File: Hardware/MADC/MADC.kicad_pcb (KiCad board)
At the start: 2 copper layers, 20 x 20 mm, 34 parts, among them J1 Conn_02x04_Counter_Clockwise, J3 Conn_02x03_Counter_Clockwise, U1 LM311PWR, U2 OPA192IDBVT, U3 OPA140AIDBVT, U4 OPA2192IDGKT, U5 DG419LEUA, U6 DG211BDQ-T1-E3

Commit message: PCB
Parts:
- removed the C8 at (142.5, 106.9)
- added C1: 0.1u, Capacitor_SMD:C_0402_1005Metric_Pad0.74x0.62mm_HandSolder, F.Cu at (148.1, 92.2)
- added C10: 0.1u, Capacitor_SMD:C_0402_1005Metric_Pad0.74x0.62mm_HandSolder, F.Cu at (147.4, 98.6)
- added C11: 0.1u, Capacitor_SMD:C_0402_1005Metric_Pad0.74x0.62mm_HandSolder, F.Cu at (139.4, 91.6)
- added C2: 0.1u, Capacitor_SMD:C_0402_1005Metric_Pad0.74x0.62mm_HandSolder, F.Cu at (145.4, 101.7)
- added C3: 0.1u, Capacitor_SMD:C_0402_1005Metric_Pad0.74x0.62mm_HandSolder, F.Cu at (147.4, 95.5)
- added C4: 0.1u, Capacitor_SMD:C_0402_1005Metric_Pad0.74x0.62mm_HandSolder, F.Cu at (139.8, 99.9)
- added C5: 0.1u, Capacitor_SMD:C_0402_1005Metric_Pad0.74x0.62mm_HandSolder, B.Cu at (146.2, 91.9)
- C12: renamed from C2; moved to F.Cu
- C8: renamed from C7; moved to F.Cu
- D1, D2: value BAV21W-E3-08 -> 1N4448WT; footprint Diode_SMD:D_SOD-123 -> Diode_SMD:D_SOD-323
- J2: renamed from J3; footprint Connector_PinHeader_1.27mm:PinHeader_2x03_P1.27mm_Vertical_SMD -> Connector_PinHeader_1.27mm:PinHeader_2x04_P1.27mm_Vertical_SMD
- R10: renamed from R6; moved to F.Cu
- R4: renamed from R9; moved to B.Cu
- RN1: moved to B.Cu
- RN2: renamed from RN3; moved to B.Cu
- U2: renamed from U5; moved to F.Cu
- moved R1 28.9 mm to (134.9, 89.3), turned to -90 degrees
- moved R2 27.1 mm to (135.9, 93.5), turned to 180 degrees
- moved C7 25.8 mm to (138.2, 93.5), turned to 180 degrees
- moved C6 24.4 mm to (134.9, 91.6), turned to 90 degrees
- moved C9 13.4 mm to (140.1, 95.9), turned to -90 degrees
- moved C8 7.55 mm to (137.2, 88.1), turned to 180 degrees
- moved RN1 7.54 mm to (143.8, 93.3), turned to 90 degrees
- moved C12 7.11 mm to (147.3, 86.5), turned to 90 degrees
- moved R5 6.16 mm to (146.3, 86.5), turned to 90 degrees
- moved C13 6.04 mm to (140.1, 86.2)
- moved R6 5.89 mm to (141.1, 86.2), turned to 90 degrees
- moved U4 4.38 mm to (137.2, 90.9), turned to 90 degrees
- moved R11 3.96 mm to (149.2, 96.6)
- moved RN2 3.92 mm to (143.8, 99.4), turned to 180 degrees
- moved R10 3.91 mm to (151.5, 96.6), turned to -90 degrees
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- renumbered C3 to C13, C4 to C14, C1 to C15, C5 to C6, C6 to C7, R11 to R1, R5 to R11, R4 to R12, R12 to R2, R10 to R3, R7 to R5, R8 to R6, R2 to R7, R1 to R8, R3 to R9, RN2 to RN3, U6 to U1, U4 to U3, U3 to U4, U2 to U5, U1 to U6
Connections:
- J1 pad 2: /AD_IRN -> +3.3V
- J1 pad 3: /AD_ID -> /AD_CMP
- J1 pad 4: /AD_IIN -> /AD_IRN
- J1 pad 6: /AD_IRP -> /AD_IIN
- J1 pad 7: /AD_CMP -> /AD_IRP
- J1 pad 8: +3.3V -> /AD_ID
- J2 pad 2: /AD_IN -> GNDA
- J2 pad 3: GNDA -> /AD_IN
- J2 pad 4: VCC -> GNDA
- J2 pad 5: VEE -> /AD_IN
- J2 pad 6: -7V -> VCC
- U2 pad 1: unconnected-(U5-Pad1) -> Net-(U3A-+)
- U3 pad 3: unconnected-(U4A-+-Pad3) -> Net-(U3A-+)
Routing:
- net VCC: track 0.00 -> 57.4 mm, vias 0 -> 6
- net VEE: track 0.00 -> 46.3 mm, vias 0 -> 6
- net +3.3V: track 0.00 -> 40.4 mm, vias 0 -> 6
- net GNDA: track 0.00 -> 31.1 mm, vias 0 -> 20
- net Net-(C8-Pad2): track 0.00 -> 31.0 mm, vias 0 -> 2
- net Net-(U4--): track 0.00 -> 25.1 mm
- net /AD_REF+: track 0.00 -> 20.9 mm, vias 0 -> 1
- net /AD_REF-: track 0.00 -> 17.0 mm, vias 0 -> 1
- net /AD_IN: track 0.00 -> 16.2 mm
- net /AD_IRN: track 0.00 -> 16.2 mm, vias 0 -> 1
- net Net-(D1-A): track 0.00 -> 15.7 mm, vias 0 -> 1
- net Net-(D1-K): track 0.00 -> 15.1 mm, vias 0 -> 2
- net /AD_IIN: track 0.00 -> 13.8 mm, vias 0 -> 1
- net -7V: track 0.00 -> 13.8 mm, vias 0 -> 1
- net /SW_VRH: track 0.00 -> 13.5 mm, vias 0 -> 1
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- added copper zone on B.Cu, net +3.3V
- added copper zone on In2.Cu, net +3.3V
- added copper zone on B.Cu, net GNDA
- added copper zone on F.Cu, net GNDA
- added copper zone on In1.Cu, net GNDA
- added copper zone on B.Cu, net GNDD
- added copper zone on F.Cu, net GNDD
- added copper zone on In1.Cu, net GNDD
- added copper zone on In2.Cu, net VCC
- added copper zone on In2.Cu, net VEE
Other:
- copper layers 2 -> 4

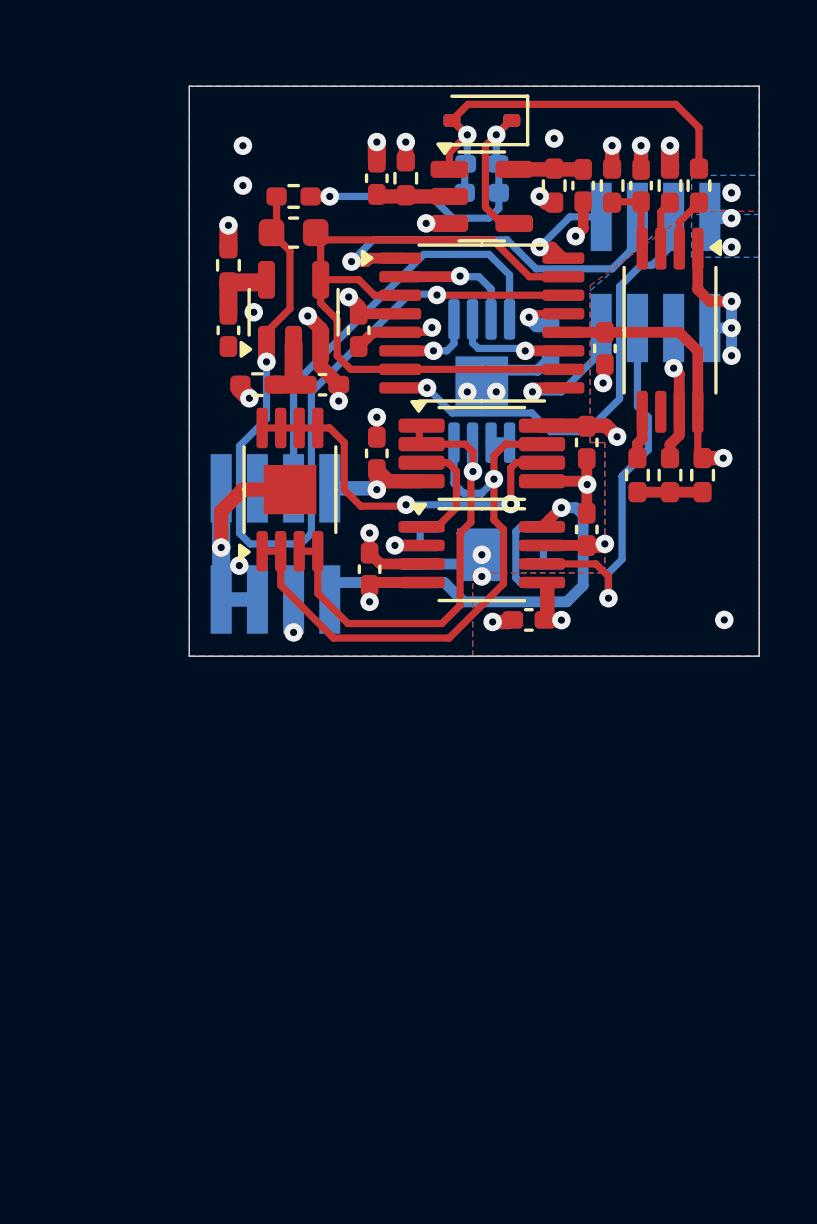
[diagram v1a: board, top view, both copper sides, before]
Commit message: MADC module send to production
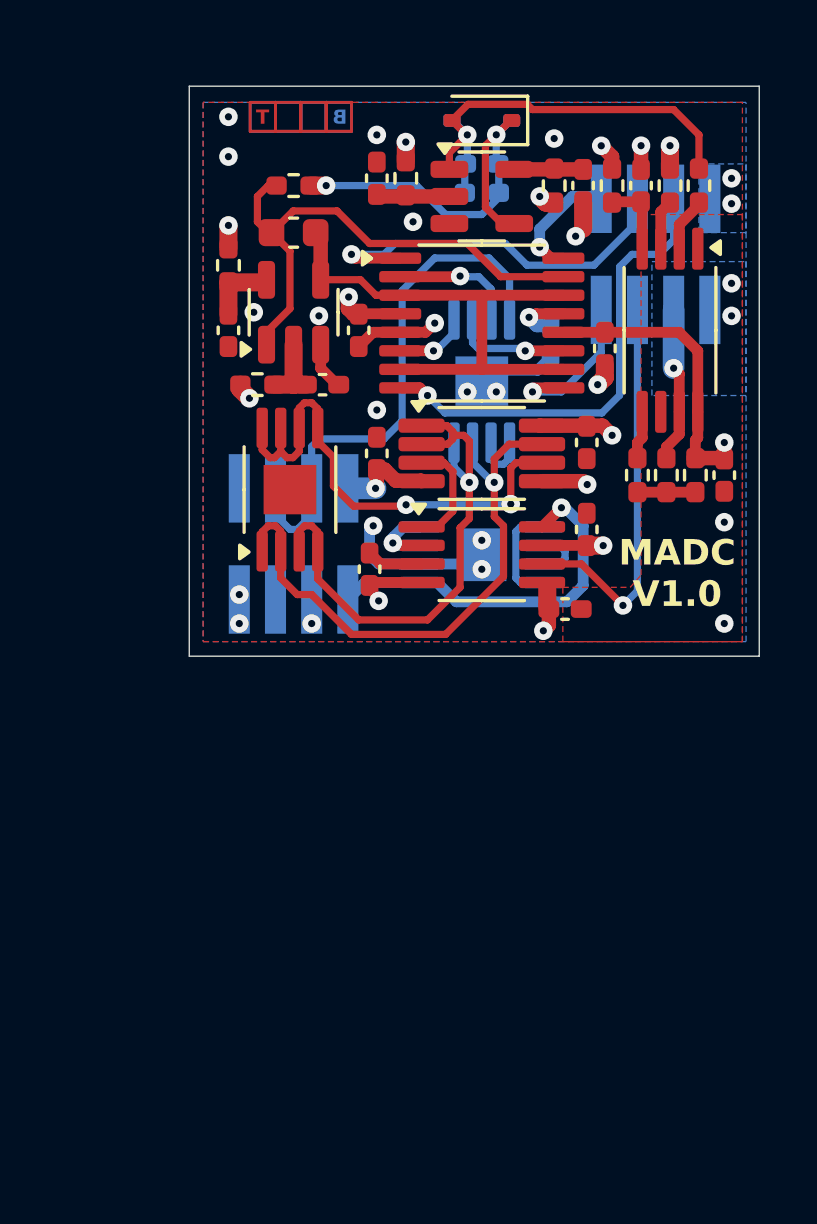
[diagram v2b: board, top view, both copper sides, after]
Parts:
- added C16: 0.1u, Capacitor_SMD:C_0402_1005Metric_Pad0.74x0.62mm_HandSolder, F.Cu at (152.3, 96.6)
- J1: value Conn_02x04_Counter_Clockwise -> 62130821021
- J2: value Conn_02x03_Counter_Clockwise -> 62130821021
- moved C2 1.33 mm to (146.7, 101.3), turned to 180 degrees
- moved J1 0.63 mm to (149.9, 88.9)
- moved J2 0.63 mm to (137.2, 99.1)
- moved R3 0.38 mm to (137.2, 86.5)
- moved R10 0.25 mm to (151.3, 96.6)
- moved R12 0.13 mm to (150.2, 96.6)
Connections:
- net -7V renamed VREF
- RN3 pad 1: /AD_REF+ -> /AD_REF-
- RN3 pad 2: /AD_REF+ -> /AD_REF-
- RN3 pad 3: /AD_REF- -> /AD_REF+
- RN3 pad 4: /AD_REF- -> /AD_REF+
- U1 pad 14: Net-(C8-Pad2) -> Net-(U4--)
- U1 pad 15: Net-(U4--) -> Net-(C8-Pad2)
- U3 pad 1: /AD_REF- -> /AD_REF+
- U3 pad 2: /AD_REF- -> /AD_REF+
- U3 pad 7: /AD_REF+ -> /AD_REF-
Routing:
- net GNDA: track 31.1 -> 18.0 mm, vias 20 -> 19
- net Net-(C8-Pad2): track 31.0 -> 18.5 mm, vias 2 -> 0
- net Net-(U4--): track 25.1 -> 18.8 mm
- net Net-(U3B--): track 13.3 -> 17.5 mm
- net /AD_REF-: track 17.0 -> 20.5 mm
- net GNDD: track 6.86 -> 3.44 mm, vias 6 -> 5
- net /AD_IN: track 16.2 -> 19.1 mm
- net VCC: track 57.4 -> 54.9 mm
- net Net-(RN2-Pad7): track 1.59 -> 3.34 mm
- net /AD_REF+: track 20.9 -> 19.4 mm
- net /AD_ID: track 3.59 -> 4.93 mm
- net Net-(RN1-Pad1): track 0.65 -> 1.94 mm
- net Net-(RN2-Pad2): track 0.65 -> 1.94 mm
- net VEE: track 46.3 -> 45.1 mm
- net VREF: track 13.8 -> 12.6 mm
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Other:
- board text added: "2"
- board text added: "3"
- board text added: "B"
- board text added: "MADC V1.0"
- board text added: "T"
